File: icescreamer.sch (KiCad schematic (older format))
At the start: 35 parts

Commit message: schematic almost finished
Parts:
- added 0.1uF, C? (x2): C, ~, symbol C
- added C?: CAPAPOL, ~, symbol CAPAPOL
- added CON?: BARREL_JACK, symbol BARREL_JACK
- added J?: JACK_2P, ~, symbol JACK_2P
- added P?: CONN_2, symbol CONN_2
- added U?: TLE2426, ~, symbol TLE2426
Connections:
- wire segments 68 -> 88
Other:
- moved on the sheet: C?, Q?, R?

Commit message: eeeeinnnn?
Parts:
- removed J?: JACK_2P, ~, symbol JACK_2P
- added J? (x2): JACK_3P, ~, symbol JACK_3P
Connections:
- wire segments 88 -> 94
- no-connect marks 0 -> 2
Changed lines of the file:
@@
 LIBS:uC3Moy-cache
 LIBS:icescreamer
+LIBS:icescreamer-cache
 EELAYER 27 0
 EELAYER END
@@
 	5750 7000 5950 7000
 $Comp
-L JACK_2P J?
-U 1 1 5519D1CE
+L JACK_3P J?
+U 1 1 5519D436
 P 1350 4450
 F 0 "J?" H 1200 4800 60  0000 C CNN
-F 1 "JACK_2P" H 1200 4700 60  0000 C CNN
+F 1 "JACK_3P" H 1200 4700 60  0000 C CNN
 F 2 "~" H 1350 4450 60  0000 C CNN
 F 3 "~" H 1350 4450 60  0000 C CNN
@@
 	1    0    0    -1
 $EndComp
+$Comp
+L JACK_3P J?
+U 1 1 5519D445
+P 9950 4600
+F 0 "J?" H 9800 4950 60  0000 C CNN
+F 1 "JACK_3P" H 9800 4850 60  0000 C CNN
+F 2 "~" H 9950 4600 60  0000 C CNN
+F 3 "~" H 9950 4600 60  0000 C CNN
+	1    9950 4600
+	-1   0    0    -1
+$EndComp
+NoConn ~ 9500 4600
+NoConn ~ 9500 4450
+$Comp
+L -5V #PWR?
+U 1 1 5519D536
+P 10350 5150
+F 0 "#PWR?" H 10350 5290 20  0001 C CNN
+F 1 "-5V" H 10350 5260 30  0000 C CNN
+F 2 "" H 10350 5150 60  0000 C CNN
+F 3 "" H 10350 5150 60  0000 C CNN
+	1    10350 5150
+	-1   0    0    1
+$EndComp
+Wire Wire Line
+	10350 5050 10350 5150
+$Comp
+L -5V #PWR?
+U 1 1 5519D5AB
+P 950 5000
+F 0 "#PWR?" H 950 5140 20  0001 C CNN
+F 1 "-5V" H 950 5110 30  0000 C CNN
+F 2 "" H 950 5000 60  0000 C CNN
+F 3 "" H 950 5000 60  0000 C CNN
+	1    950  5000
+	-1   0    0    1
+$EndComp
+Wire Wire Line
+	950  4900 950  5000
+Wire Wire Line
+	3100 6450 3100 5600
+Wire Wire Line
+	3100 5600 2000 5600
+Wire Wire Line
+	2000 5600 2000 4300
+Wire Wire Line
+	2000 4300 1800 4300
+Connection ~ 3100 6450
 $EndSCHEMATC

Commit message: after some night-working!
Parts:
- removed C?: 0.1uF, ~, symbol C
- removed R?: 0R, ~, symbol R
- removed U?: TLE2426, ~, symbol TLE2426
- added C10: 1uF, ~, symbol C
- added D3: LED, ~, symbol LED
- added D4: DIODE, ~, symbol DIODE
- added R11: 4K7, ~, symbol R
- added SW1: 3PDT, ~, symbol 3PDT
- added U2: TLE2426NR, ~, symbol TLE2426NR
- C1: renamed from C?; value 0.02 -> 0.02uF
- C12, C13: renamed from C?; value C -> 0.1uF
- C7: renamed from C?; value CAPAPOL -> 220uF
- C8: renamed from 0.1uF; value C -> 0.1uF
- gave numbers to parts that had none: 35
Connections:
- net labels added: FX in, FX out
- net labels removed: BYPASS_STAGE, FROM_BYPASS, INPUT
- wire segments 94 -> 101
- no-connect marks 2 -> 5
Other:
- moved on the sheet: C1, C11, C12, C13, C14, C2, C3, C4, C5, C6, C7, C8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

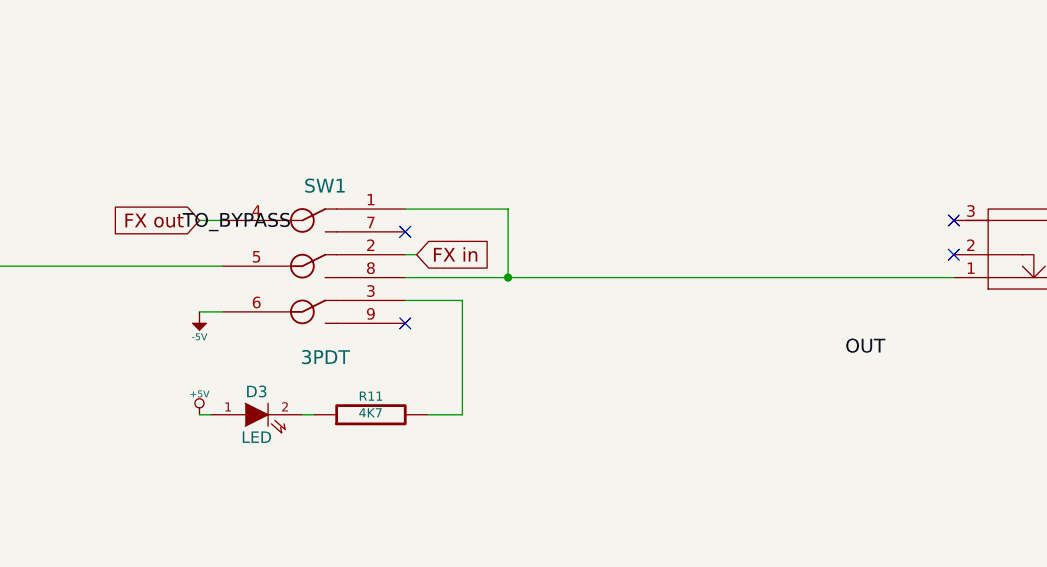
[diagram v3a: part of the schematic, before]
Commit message: Correct issues in schematic, add pcb file
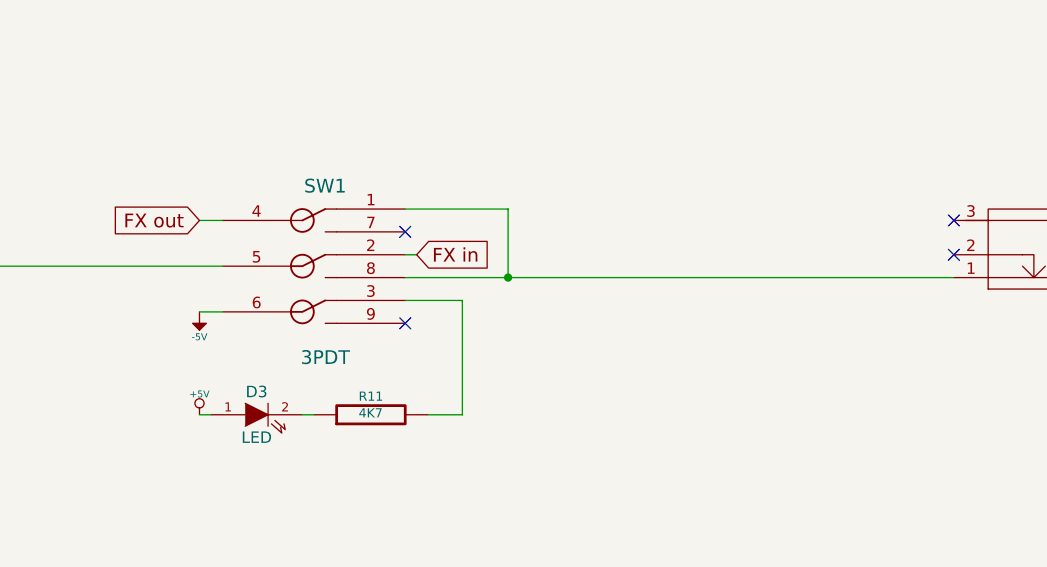
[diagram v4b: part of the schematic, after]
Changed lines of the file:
@@
 LIBS:contrib
 LIBS:valves
-LIBS:uC3Moy-cache
-LIBS:icescreamer
+LIBS:kicad-library
 LIBS:icescreamer-cache
 EELAYER 27 0
@@
 Sheet 1 1
 Title "TubeScreamer"
-Date "31 mar 2015"
+Date "5 apr 2015"
 Rev "0.1"
 Comp "DEF"
@@
 	1    0    0    -1
 $EndComp
-Text Label 8300 5200 2    60   ~ 0
-TO_BYPASS
 $Comp
 L R R4
@@
 	1    0    0    -1
 $EndComp
-Text Label 10900 5750 2    60   ~ 0
-OUT
 $Comp
 L -5V #PWR012

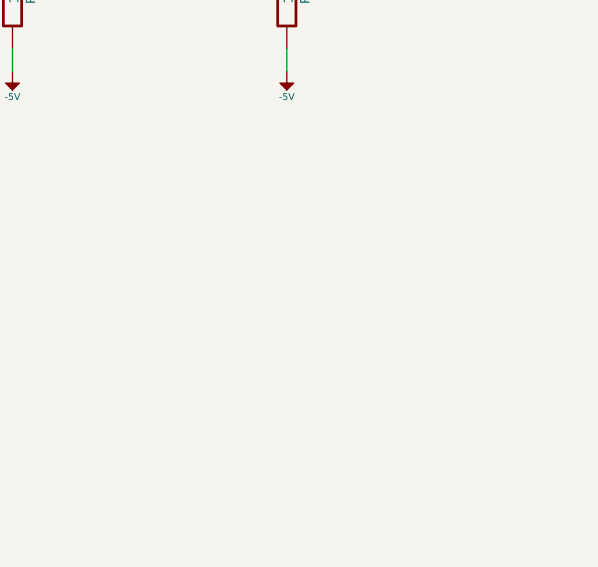
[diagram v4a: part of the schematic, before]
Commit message: Add comment about recommended transistors
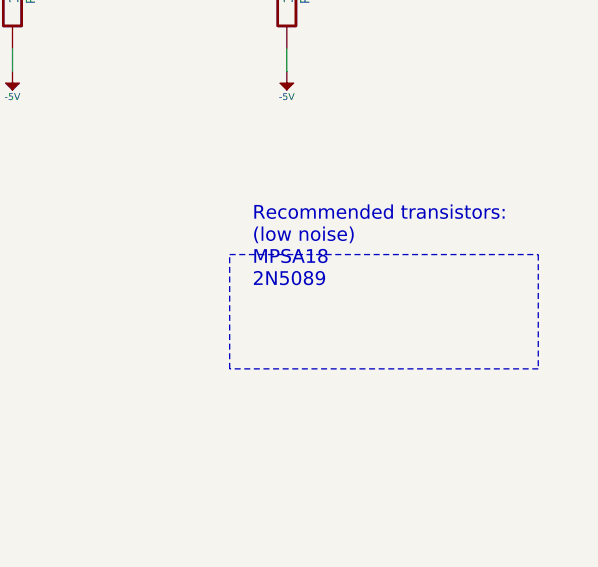
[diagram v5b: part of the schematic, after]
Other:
- note added: "Recommended transistors:\n(low noise)\nMPSA18\n2N5089"
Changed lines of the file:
@@
 Sheet 1 1
 Title "TubeScreamer"
-Date "5 apr 2015"
+Date "6 apr 2015"
 Rev "0.1"
 Comp "DEF"
@@
 Wire Wire Line
 	9800 9300 9800 9200
+Text Notes 13500 4200 0    60   ~ 0
+Recommended transistors:\n(low noise)\nMPSA18\n2N5089
+Wire Notes Line
+	13400 4050 14750 4050
+Wire Notes Line
+	14750 4050 14750 4550
+Wire Notes Line
+	14750 4550 13400 4550
+Wire Notes Line
+	13400 4550 13400 4050
 $EndSCHEMATC

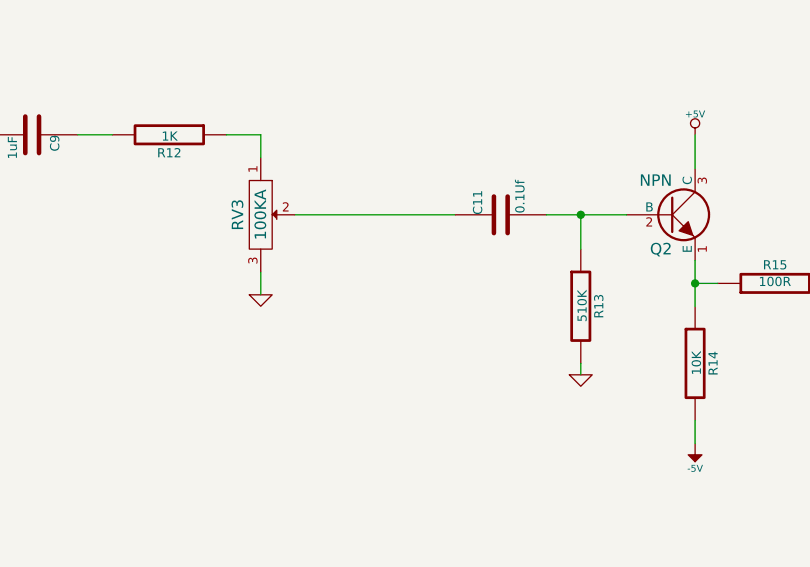
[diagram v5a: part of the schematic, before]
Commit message: Add resistor to convert volume pot from linear to log
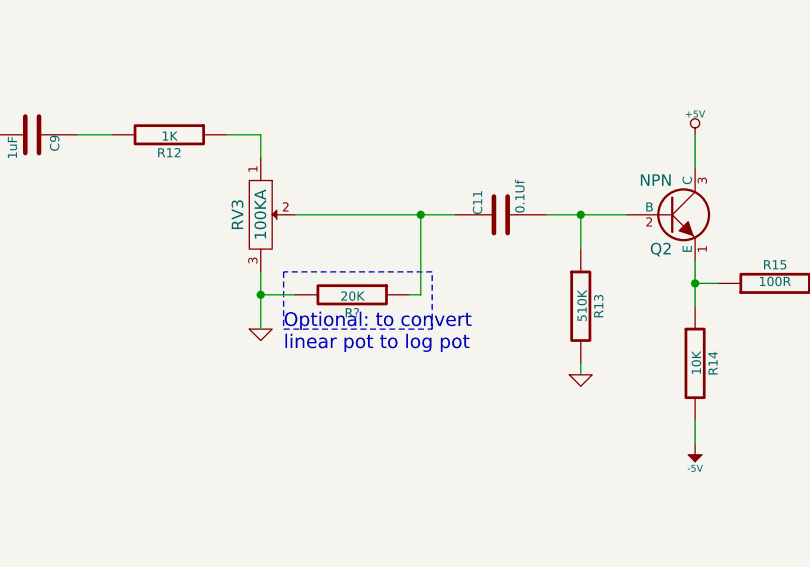
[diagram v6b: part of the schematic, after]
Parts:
- added R?: 20K, ~, symbol R
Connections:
- net GND: now also R?.2
- net at C11.1, RV3.2: now also R?.1
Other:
- note added: "Optional: to convert\nlinear pot to log pot"
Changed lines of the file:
@@
 Sheet 1 1
 Title "TubeScreamer"
-Date "6 apr 2015"
+Date "7 apr 2015"
 Rev "0.1"
 Comp "DEF"
@@
 L GND #PWR015
 U 1 1 5511B926
-P 10550 2600
-F 0 "#PWR015" H 10550 2600 30  0001 C CNN
-F 1 "GND" H 10550 2530 30  0001 C CNN
-F 2 "" H 10550 2600 60  0000 C CNN
-F 3 "" H 10550 2600 60  0000 C CNN
-	1    10550 2600
+P 10550 2750
+F 0 "#PWR015" H 10550 2750 30  0001 C CNN
+F 1 "GND" H 10550 2680 30  0001 C CNN
+F 2 "" H 10550 2750 60  0000 C CNN
+F 3 "" H 10550 2750 60  0000 C CNN
+	1    10550 2750
 	1    0    0    -1
 $EndComp
@@
 	9750 1900 9900 1900
 Wire Wire Line
-	10550 1900 10400 1900
-Wire Wire Line
 	8050 2000 8050 2800
 Wire Wire Line
@@
 	5900 1800 6150 1800
 Wire Wire Line
-	10550 2500 10550 2600
+	10550 2500 10550 2750
 Wire Wire Line
 	11800 2250 12150 2250
@@
 Wire Notes Line
 	13400 4550 13400 4050
+$Comp
+L R R?
+U 1 1 5524175C
+P 10950 2600
+F 0 "R?" V 11030 2600 40  0000 C CNN
+F 1 "20K" V 10957 2601 40  0000 C CNN
+F 2 "~" V 10880 2600 30  0000 C CNN
+F 3 "~" H 10950 2600 30  0000 C CNN
+	1    10950 2600
+	0    1    1    0
+$EndComp
+Connection ~ 11250 2250
+Text Notes 10650 2850 0    60   ~ 0
+Optional: to convert\nlinear pot to log pot
+Wire Wire Line
+	10550 1900 10400 1900
+Wire Wire Line
+	11250 2600 11200 2600
+Wire Wire Line
+	11250 2600 11250 2250
+Wire Wire Line
+	10700 2600 10550 2600
+Connection ~ 10550 2600
+Wire Notes Line
+	10650 2500 10650 2750
+Wire Notes Line
+	10650 2750 11300 2750
+Wire Notes Line
+	11300 2750 11300 2500
+Wire Notes Line
+	11300 2500 10650 2500
 $EndSCHEMATC

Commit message: Update jack symbol in schematic
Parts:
- removed J1, J2: JACK_3P, ~, symbol JACK_3P
- added J? (x2): JACK, ~, symbol CONNECTORS_JACK_FEMALE_STEREO_6_PINS
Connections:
- no-connect marks 5 -> 9
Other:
- note added: "INPUT"
- note added: "OUTPUT JACK"
- note added: "POWER INPUT"
- moved on the sheet: CON1, D3, P1, R11, SW1

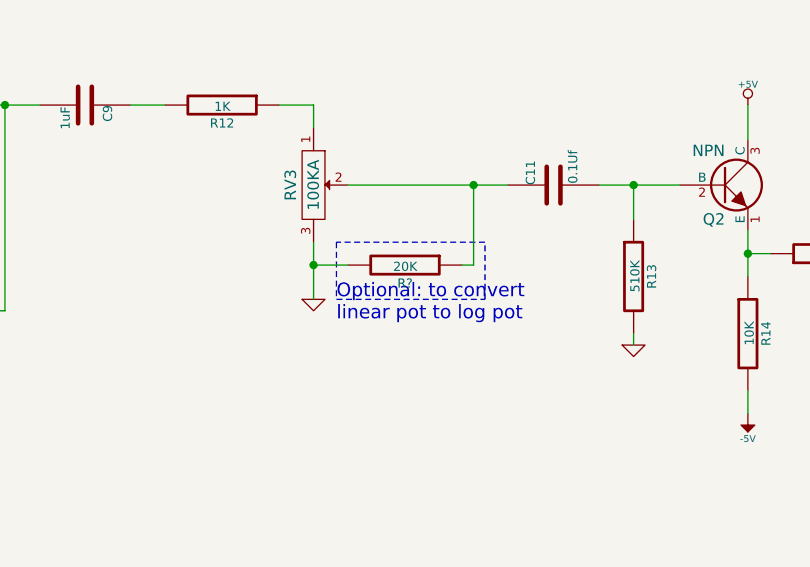
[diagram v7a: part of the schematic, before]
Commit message: Update footprint for female jack in netlist
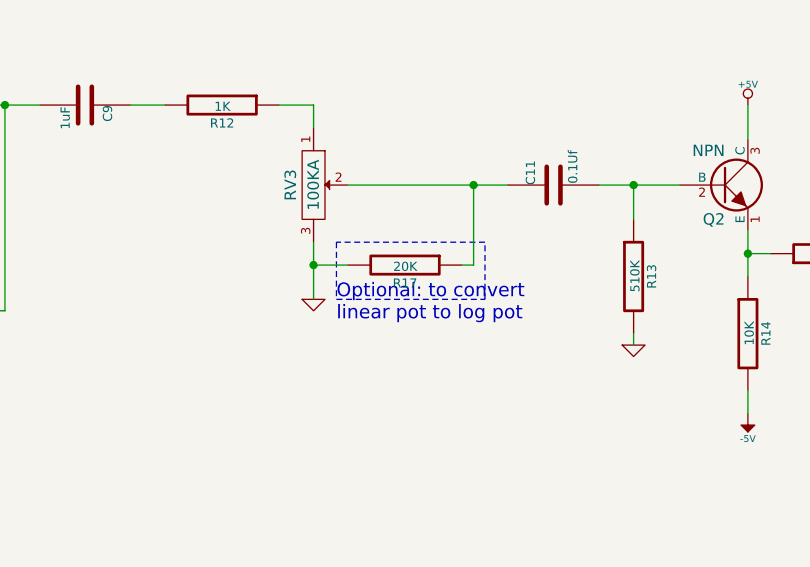
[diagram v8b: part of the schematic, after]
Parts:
- gave numbers to parts that had none: 3
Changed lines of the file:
@@
 	5650 3050 6000 3050
 $Comp
-L +5V #PWR025
+L +5V #PWR024
 U 1 1 5519F033
 P 12450 1900
-F 0 "#PWR025" H 12450 1990 20  0001 C CNN
+F 0 "#PWR024" H 12450 1990 20  0001 C CNN
 F 1 "+5V" H 12450 1990 30  0000 C CNN
 F 2 "" H 12450 1900 60  0000 C CNN
@@
 	12450 1900 12450 2050
 $Comp
-L +5V #PWR026
+L +5V #PWR025
 U 1 1 5519F0B4
 P 8550 1450
-F 0 "#PWR026" H 8550 1540 20  0001 C CNN
+F 0 "#PWR025" H 8550 1540 20  0001 C CNN
 F 1 "+5V" H 8550 1540 30  0000 C CNN
 F 2 "" H 8550 1450 60  0000 C CNN
@@
 	8550 1450 8550 1500
 $Comp
-L +5V #PWR027
+L +5V #PWR026
 U 1 1 5519F135
 P 6700 5000
-F 0 "#PWR027" H 6700 5090 20  0001 C CNN
+F 0 "#PWR026" H 6700 5090 20  0001 C CNN
 F 1 "+5V" H 6700 5090 30  0000 C CNN
 F 2 "" H 6700 5000 60  0000 C CNN
@@
 $EndComp
 $Comp
-L +5V #PWR028
+L +5V #PWR027
 U 1 1 5519E78F
 P 7950 7200
-F 0 "#PWR028" H 7950 7290 20  0001 C CNN
+F 0 "#PWR027" H 7950 7290 20  0001 C CNN
 F 1 "+5V" H 7950 7290 30  0000 C CNN
 F 2 "" H 7950 7200 60  0000 C CNN
@@
 $EndComp
 $Comp
-L GND #PWR029
+L GND #PWR028
 U 1 1 5519EBF0
 P 11050 8850
-F 0 "#PWR029" H 11050 8850 30  0001 C CNN
+F 0 "#PWR028" H 11050 8850 30  0001 C CNN
 F 1 "GND" H 11050 8780 30  0001 C CNN
 F 2 "" H 11050 8850 60  0000 C CNN
@@
 	11050 8800 11050 8850
 $Comp
-L +5V #PWR030
+L +5V #PWR029
 U 1 1 5519EC6D
 P 11050 8600
-F 0 "#PWR030" H 11050 8690 20  0001 C CNN
+F 0 "#PWR029" H 11050 8690 20  0001 C CNN
 F 1 "+5V" H 11050 8690 30  0000 C CNN
 F 2 "" H 11050 8600 60  0000 C CNN
@@
 	11050 8600 10950 8600
 $Comp
-L -5V #PWR031
+L -5V #PWR030
 U 1 1 5519ECEC
 P 11050 8700
-F 0 "#PWR031" H 11050 8840 20  0001 C CNN
+F 0 "#PWR030" H 11050 8840 20  0001 C CNN
 F 1 "-5V" H 11050 8810 30  0000 C CNN
 F 2 "" H 11050 8700 60  0000 C CNN
@@
 	9800 8800 9900 8800
 $Comp
-L -5V #PWR032
+L -5V #PWR031
 U 1 1 5519EE71
 P 9800 9300
-F 0 "#PWR032" H 9800 9440 20  0001 C CNN
+F 0 "#PWR031" H 9800 9440 20  0001 C CNN
 F 1 "-5V" H 9800 9410 30  0000 C CNN
 F 2 "" H 9800 9300 60  0000 C CNN
@@
 	13400 4550 13400 4050
 $Comp
-L R R?
+L R R17
 U 1 1 5524175C
 P 10950 2600
-F 0 "R?" V 11030 2600 40  0000 C CNN
+F 0 "R17" V 11030 2600 40  0000 C CNN
 F 1 "20K" V 10957 2601 40  0000 C CNN
 F 2 "~" V 10880 2600 30  0000 C CNN
@@
 	11300 2500 10650 2500
 $Comp
-L CONNECTORS_JACK_FEMALE_STEREO_6_PINS J?
+L CONNECTORS_JACK_FEMALE_STEREO_6_PINS J1
 U 1 1 5524220A
 P 6350 6400
-F 0 "J?" H 5750 5950 60  0000 C CNN
+F 0 "J1" H 5750 5950 60  0000 C CNN
 F 1 "JACK" H 5850 6700 60  0000 C CNN
 F 2 "~" H 6800 6350 60  0000 C CNN
@@
 Connection ~ 7300 6650
 $Comp
-L CONNECTORS_JACK_FEMALE_STEREO_6_PINS J?
+L CONNECTORS_JACK_FEMALE_STEREO_6_PINS J2
 U 1 1 55242A87
 P 10450 6450
-F 0 "J?" H 9850 6000 60  0000 C CNN
+F 0 "J2" H 9850 6000 60  0000 C CNN
 F 1 "JACK" H 9950 6750 60  0000 C CNN
 F 2 "~" H 10900 6400 60  0000 C CNN
